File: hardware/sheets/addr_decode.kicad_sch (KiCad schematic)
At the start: 13 parts, among them U1 74HC138, U2 74HC00, U3 74HC32, U4 74HC32, U5 74LVC125A

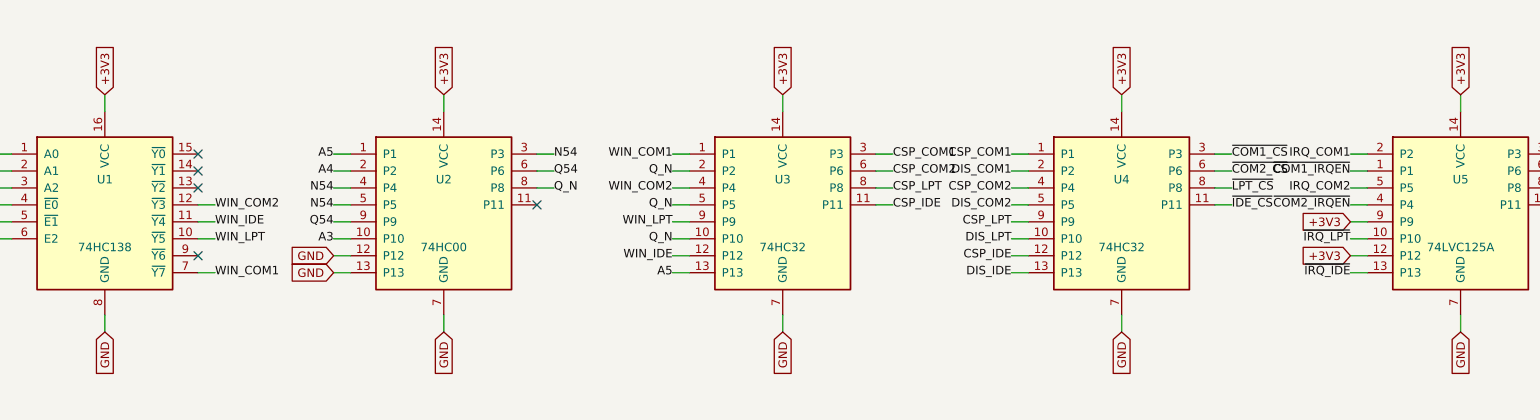
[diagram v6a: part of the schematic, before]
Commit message: KiCad 10 symbol support: read sharded .kicad_symdir libraries
The KiCad snap (which supplied the KiCad 9 monolithic .kicad_sym libs)
is gone; the KiCad 10 AppImage ships its libraries in the new sharded
format instead: <Lib>.kicad_symdir/ directories of one-symbol files.

- mxsch: lib_source() resolves a .kicad_sym path to the file or its
  .kicad_symdir sibling; SymbolLib.load() loads every file in a symdir
  (extends resolution runs after all files, since base and derived
  symbols live in separate files); kicad_symdir() falls back to
  ~/.local/share/kicad/<ver>/symbols (populated once from the AppImage)
- build/pins/gensym: route existence checks + copy_symbol through it
- power/supervisor: USB-C/USB-A shield pin renamed S1/5 -> SH in the
  KiCad 10 libs (the one real symbol-content change; still GND)
- selftest: netlist checker now tolerates KiCad 10's multiline netlist
  format (it silently found nothing since the CLI moved to 10)
- regenerate all sheets + mini-xt.kicad_sym from KiCad 10 sources: the
  churn is embedded-symbol format tokens only. Verified: ERC 0/0,
  before/after netlists have identical net->node sets (736 nets, only
  the shield-pin rename), double-build stays byte-identical, all seven
  custom symbols pin-identical after gensym regen.

Co-Authored-By: Claude Fable 5 <noreply@anthropic.com>
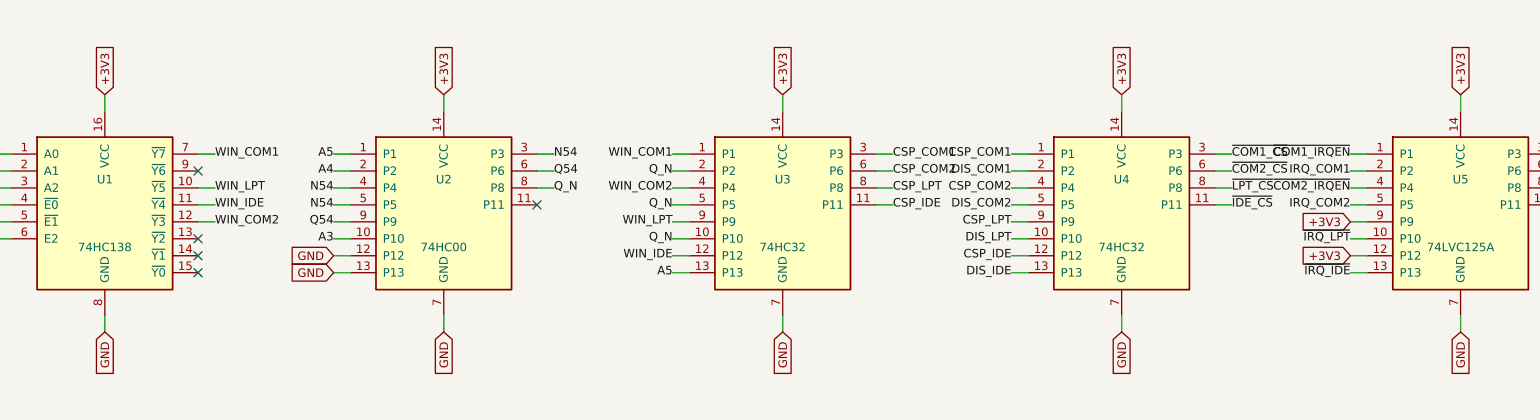
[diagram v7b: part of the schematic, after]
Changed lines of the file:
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@@
 	(wire
 		(pts
-			(xy 115.57 85.09)
-			(xy 118.11 85.09)
+			(xy 115.57 67.31)
+			(xy 118.11 67.31)
 		)
 		(stroke
@@
 	)
 	(label "WIN_COM1"
-		(at 118.11 85.09 0)
+		(at 118.11 67.31 0)
+		(effects
+			(font
+				(size 1.27 1.27)
+			)
+		)
+	)
+	(wire
+		(pts
+			(xy 115.57 77.47)
+			(xy 118.11 77.47)
+		)
+		(stroke
+			(width 0)
+			(type default)
+		)
+	)
+	(label "WIN_COM2"
+		(at 118.11 77.47 0)
+		(effects
+			(font
+				(size 1.27 1.27)
+			)
+		)
+	)
+	(wire
+		(pts
+			(xy 115.57 72.39)
+			(xy 118.11 72.39)
+		)
+		(stroke
+			(width 0)
+			(type default)
+		)
+	)
+	(label "WIN_LPT"
+		(at 118.11 72.39 0)
 		(effects
 			(font
@@
 		)
 	)
-	(label "WIN_COM2"
+	(label "WIN_IDE"
 		(at 118.11 74.93 0)
 		(effects
@@
 		)
 	)
-	(wire
-		(pts
-			(xy 115.57 80.01)
-			(xy 118.11 80.01)
-		)
-		(stroke
-			(width 0)
-			(type default)
-		)
-	)
-	(label "WIN_LPT"
-		(at 118.11 80.01 0)
-		(effects
-			(font
-				(size 1.27 1.27)
-			)
-		)
-	)
-	(wire
-		(pts
-			(xy 115.57 77.47)
-			(xy 118.11 77.47)
-		)
-		(stroke
-			(width 0)
-			(type default)
-		)
-	)
-	(label "WIN_IDE"
-		(at 118.11 77.47 0)
-		(effects
-			(font
-				(size 1.27 1.27)
-			)
-		)
-	)
 	(no_connect
-		(at 115.57 67.31)
+		(at 115.57 85.09)
+	)
+	(no_connect
+		(at 115.57 82.55)
+	)
+	(no_connect
+		(at 115.57 80.01)
 	)
 	(no_connect
 		(at 115.57 69.85)
 	)
-	(no_connect
-		(at 115.57 72.39)
-	)
-	(no_connect
-		(at 115.57 82.55)
-	)
 	(wire
 		(pts
@@
 	(wire
 		(pts
+			(xy 290.83 67.31)
+			(xy 288.29 67.31)
+		)
+		(stroke
+			(width 0)
+			(type default)
+		)
+	)
+	(label "~{COM1_IRQEN}"
+		(at 288.29 67.31 180)
+		(effects
+			(font
+				(size 1.27 1.27)
+			)
+		)
+	)
+	(wire
+		(pts
 			(xy 290.83 69.85)
 			(xy 288.29 69.85)
@@
 		)
 	)
-	(label "~{COM1_IRQEN}"
+	(label "IRQ_COM1"
 		(at 288.29 69.85 180)
-		(effects
-			(font
-				(size 1.27 1.27)
-			)
-		)
-	)
-	(wire
-		(pts
-			(xy 290.83 67.31)
-			(xy 288.29 67.31)
-		)
-		(stroke
-			(width 0)
-			(type default)
-		)
-	)
-	(label "IRQ_COM1"
-		(at 288.29 67.31 180)
 		(effects
 			(font
@@
 	(wire
 		(pts
+			(xy 290.83 72.39)
+			(xy 288.29 72.39)
+		)
+		(stroke
+			(width 0)
+			(type default)
+		)
+	)
+	(label "~{COM2_IRQEN}"
+		(at 288.29 72.39 180)
+		(effects
+			(font
+				(size 1.27 1.27)
+			)
+		)
+	)
+	(wire
+		(pts
 			(xy 290.83 74.93)
 			(xy 288.29 74.93)
@@
 		)
 	)
-	(label "~{COM2_IRQEN}"
+	(label "IRQ_COM2"
 		(at 288.29 74.93 180)
-		(effects
-			(font
-				(size 1.27 1.27)
-			)
-		)
-	)
-	(wire
-		(pts
-			(xy 290.83 72.39)
-			(xy 288.29 72.39)
-		)
-		(stroke
-			(width 0)
-			(type default)
-		)
-	)
-	(label "IRQ_COM2"
-		(at 288.29 72.39 180)
 		(effects
 			(font
@@
 		(pin "6"
 		)
+		(pin "7"
+		)
+		(pin "9"
+		)
+		(pin "10"
+		)
+		(pin "11"
+		)
+		(pin "12"
+		)
+		(pin "13"
+		)
+		(pin "14"
+		)
 		(pin "15"
-		)
-		(pin "14"
-		)
-		(pin "13"
-		)
-		(pin "12"
-		)
-		(pin "11"
-		)
-		(pin "10"
-		)
-		(pin "9"
-		)
-		(pin "7"
 		)
 		(pin "16"
@@
 			)
 		)
+		(pin "1"
+		)
 		(pin "2"
 		)
-		(pin "1"
+		(pin "4"
 		)
 		(pin "5"
-		)
-		(pin "4"
 		)
 		(pin "9"
@@
 		(pin "1"
 		)
+		(pin "2"
+		)
 		(pin "3"
 		)
+		(pin "4"
+		)
 		(pin "5"
 		)
+		(pin "6"
+		)
 		(pin "7"
 		)
+		(pin "8"
+		)
 		(pin "9"
-		)
-		(pin "2"
-		)
-		(pin "4"
-		)
-		(pin "6"
-		)
-		(pin "8"
 		)
 		(pin "10"
@@
 			)
 		)
+		(pin "1"
+		)
+		(pin "2"
+		)
+		(pin "3"
+		)
+		(pin "4"
+		)
+		(pin "5"
+		)
+		(pin "6"
+		)
+		(pin "7"
+		)
 		(pin "8"
-		)
-		(pin "1"
-		)
-		(pin "7"
-		)
-		(pin "2"
-		)
-		(pin "6"
-		)
-		(pin "3"
-		)
-		(pin "5"
-		)
-		(pin "4"
 		)
 		(instances
@@
 			)
 		)
+		(pin "1"
+		)
+		(pin "2"
+		)
+		(pin "3"
+		)
+		(pin "4"
+		)
+		(pin "5"
+		)
+		(pin "6"
+		)
+		(pin "7"
+		)
 		(pin "8"
 		)
-		(pin "1"
-		)
-		(pin "7"
-		)
-		(pin "2"
-		)
-		(pin "6"
-		)
-		(pin "3"
-		)
-		(pin "5"
-		)
-		(pin "4"
-		)
 		(instances
